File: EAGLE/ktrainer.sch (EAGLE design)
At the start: 21 parts, among them IC1 DS3231/SO

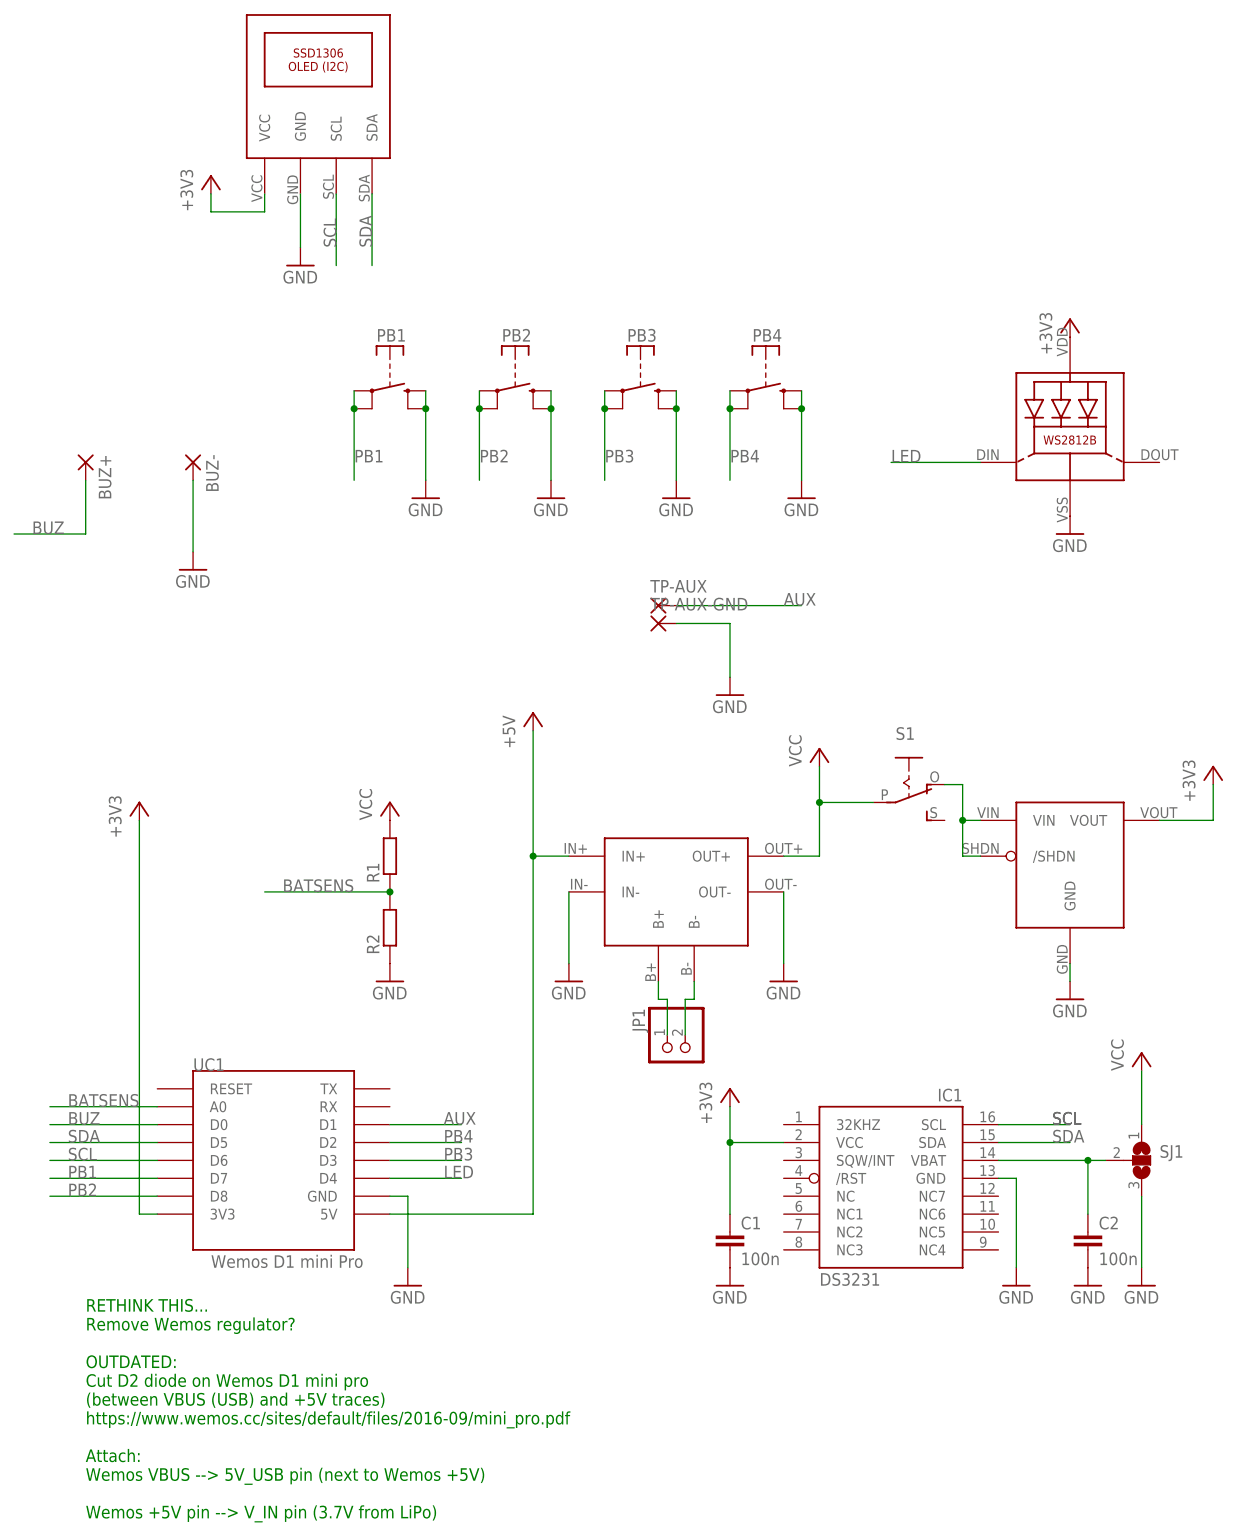
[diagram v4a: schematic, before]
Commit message: Finish work on PCB, create gerber files and order on Seeed Studio
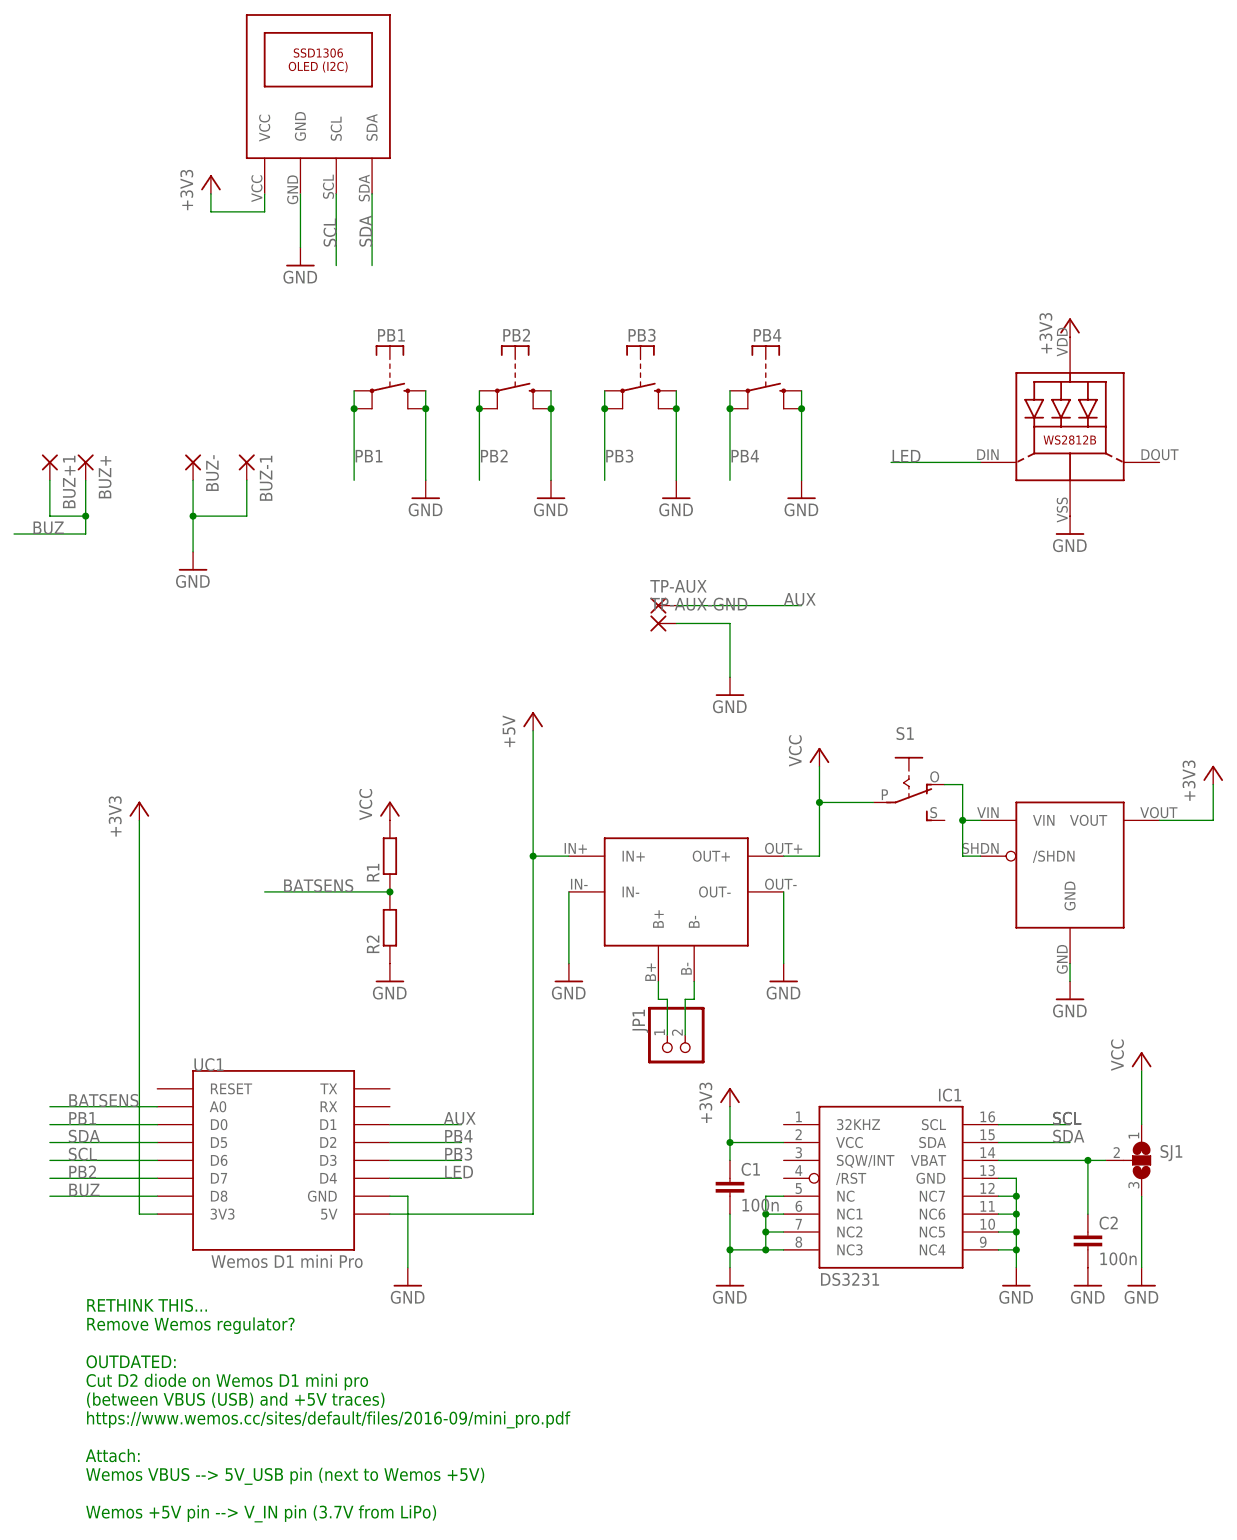
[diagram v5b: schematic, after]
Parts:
- added BUZ+1, BUZ-1: (no value), wirepad:SMD2
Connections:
- net N$6 renamed B-
- net BUZ: now also BUZ+1.P, UC1.D8; no longer UC1.D0
- net GND: now also BUZ-1.P, IC1.NC, IC1.NC1, IC1.NC2, IC1.NC3, IC1.NC4, IC1.NC5, IC1.NC6, IC1.NC7
- net PB1: now also UC1.D0; no longer UC1.D7
- net PB2: now also UC1.D7; no longer UC1.D8
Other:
- moved on the sheet: C1
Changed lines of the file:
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@@
 <part name="TP-AUX" library="wirepad" deviceset="SMD2" device=""/>
 <part name="TP-AUX-GND" library="wirepad" deviceset="SMD2" device=""/>
+<part name="BUZ+1" library="wirepad" deviceset="SMD2" device=""/>
+<part name="BUZ-1" library="wirepad" deviceset="SMD2" device=""/>
 </parts>
 <sheets>
@@
 <instance part="+3V5" gate="G$1" x="175.26" y="129.54"/>
 <instance part="P+2" gate="VCC" x="165.1" y="88.9"/>
-<instance part="C1" gate="G$1" x="106.68" y="63.5"/>
+<instance part="C1" gate="G$1" x="106.68" y="71.12"/>
 <instance part="GND12" gate="1" x="106.68" y="55.88"/>
 <instance part="C2" gate="G$1" x="157.48" y="63.5"/>
@@
 <instance part="TP-AUX" gate="1" x="96.52" y="152.4"/>
 <instance part="TP-AUX-GND" gate="1" x="96.52" y="149.86"/>
+<instance part="BUZ+1" gate="1" x="10.16" y="172.72" rot="R270"/>
+<instance part="BUZ-1" gate="1" x="38.1" y="172.72" rot="R270"/>
 </instances>
 <busses>
@@
 <pinref part="IC1" gate="G$1" pin="GND"/>
 <pinref part="GND8" gate="1" pin="GND"/>
-<wire x1="147.32" y1="58.42" x2="147.32" y2="71.12" width="0.1524" layer="91"/>
+<wire x1="147.32" y1="58.42" x2="147.32" y2="60.96" width="0.1524" layer="91"/>
+<wire x1="147.32" y1="60.96" x2="147.32" y2="63.5" width="0.1524" layer="91"/>
+<wire x1="147.32" y1="63.5" x2="147.32" y2="66.04" width="0.1524" layer="91"/>
+<wire x1="147.32" y1="66.04" x2="147.32" y2="68.58" width="0.1524" layer="91"/>
+<wire x1="147.32" y1="68.58" x2="147.32" y2="71.12" width="0.1524" layer="91"/>
 <wire x1="147.32" y1="71.12" x2="144.78" y2="71.12" width="0.1524" layer="91"/>
+<pinref part="IC1" gate="G$1" pin="NC7"/>
+<wire x1="144.78" y1="68.58" x2="147.32" y2="68.58" width="0.1524" layer="91"/>
+<pinref part="IC1" gate="G$1" pin="NC6"/>
+<wire x1="144.78" y1="66.04" x2="147.32" y2="66.04" width="0.1524" layer="91"/>
+<pinref part="IC1" gate="G$1" pin="NC5"/>
+<wire x1="144.78" y1="63.5" x2="147.32" y2="63.5" width="0.1524" layer="91"/>
+<pinref part="IC1" gate="G$1" pin="NC4"/>
+<wire x1="144.78" y1="60.96" x2="147.32" y2="60.96" width="0.1524" layer="91"/>
+<junction x="147.32" y="68.58"/>
+<junction x="147.32" y="66.04"/>
+<junction x="147.32" y="63.5"/>
+<junction x="147.32" y="60.96"/>
 </segment>
 <segment>
@@
 <pinref part="C1" gate="G$1" pin="2"/>
 <pinref part="GND12" gate="1" pin="GND"/>
+<wire x1="106.68" y1="66.04" x2="106.68" y2="60.96" width="0.1524" layer="91"/>
+<pinref part="IC1" gate="G$1" pin="NC"/>
+<wire x1="106.68" y1="60.96" x2="106.68" y2="58.42" width="0.1524" layer="91"/>
+<wire x1="114.3" y1="68.58" x2="111.76" y2="68.58" width="0.1524" layer="91"/>
+<wire x1="111.76" y1="68.58" x2="111.76" y2="66.04" width="0.1524" layer="91"/>
+<pinref part="IC1" gate="G$1" pin="NC3"/>
+<wire x1="111.76" y1="63.5" x2="111.76" y2="60.96" width="0.1524" layer="91"/>
+<wire x1="111.76" y1="60.96" x2="114.3" y2="60.96" width="0.1524" layer="91"/>
+<pinref part="IC1" gate="G$1" pin="NC2"/>
+<wire x1="114.3" y1="63.5" x2="111.76" y2="63.5" width="0.1524" layer="91"/>
+<pinref part="IC1" gate="G$1" pin="NC1"/>
+<wire x1="114.3" y1="66.04" x2="111.76" y2="66.04" width="0.1524" layer="91"/>
+<wire x1="111.76" y1="66.04" x2="111.76" y2="63.5" width="0.1524" layer="91"/>
+<wire x1="111.76" y1="60.96" x2="106.68" y2="60.96" width="0.1524" layer="91"/>
+<junction x="106.68" y="60.96"/>
+<junction x="111.76" y="60.96"/>
+<junction x="111.76" y="63.5"/>
+<junction x="111.76" y="66.04"/>
 </segment>
 <segment>
@@
 <pinref part="GND15" gate="1" pin="GND"/>
 <pinref part="BUZ-" gate="1" pin="P"/>
-<wire x1="30.48" y1="170.18" x2="30.48" y2="160.02" width="0.1524" layer="91"/>
+<wire x1="30.48" y1="170.18" x2="30.48" y2="165.1" width="0.1524" layer="91"/>
+<pinref part="BUZ-1" gate="1" pin="P"/>
+<wire x1="30.48" y1="165.1" x2="30.48" y2="160.02" width="0.1524" layer="91"/>
+<wire x1="38.1" y1="170.18" x2="38.1" y2="165.1" width="0.1524" layer="91"/>
+<wire x1="38.1" y1="165.1" x2="30.48" y2="165.1" width="0.1524" layer="91"/>
+<junction x="30.48" y="165.1"/>
 </segment>
 <segment>
@@
 </segment>
 <segment>
-<pinref part="UC1" gate="D1" pin="D7"/>
-<wire x1="25.4" y1="71.12" x2="10.16" y2="71.12" width="0.1524" layer="91"/>
-<label x="12.7" y="71.12" size="1.778" layer="95"/>
+<pinref part="UC1" gate="D1" pin="D0"/>
+<wire x1="25.4" y1="78.74" x2="10.16" y2="78.74" width="0.1524" layer="91"/>
+<label x="12.7" y="78.74" size="1.778" layer="95"/>
 </segment>
 </net>
@@
 </segment>
 <segment>
-<pinref part="UC1" gate="D1" pin="D8"/>
-<wire x1="25.4" y1="68.58" x2="10.16" y2="68.58" width="0.1524" layer="91"/>
-<label x="12.7" y="68.58" size="1.778" layer="95"/>
+<pinref part="UC1" gate="D1" pin="D7"/>
+<wire x1="25.4" y1="71.12" x2="10.16" y2="71.12" width="0.1524" layer="91"/>
+<label x="12.7" y="71.12" size="1.778" layer="95"/>
 </segment>
 </net>
@@
 <wire x1="106.68" y1="76.2" x2="114.3" y2="76.2" width="0.1524" layer="91"/>
 <pinref part="C1" gate="G$1" pin="1"/>
-<wire x1="106.68" y1="76.2" x2="106.68" y2="66.04" width="0.1524" layer="91"/>
+<wire x1="106.68" y1="76.2" x2="106.68" y2="73.66" width="0.1524" layer="91"/>
 <junction x="106.68" y="76.2"/>
 </segment>
@@
 </segment>
 </net>
-<net name="N$6" class="0">
+<net name="B-" class="0">
 <segment>
 <pinref part="JP1" gate="G$1" pin="2"/>
@@
 <pinref part="BUZ+" gate="1" pin="P"/>
 <wire x1="15.24" y1="162.56" x2="5.08" y2="162.56" width="0.1524" layer="91"/>
-<wire x1="15.24" y1="170.18" x2="15.24" y2="162.56" width="0.1524" layer="91"/>
-</segment>
-<segment>
-<pinref part="UC1" gate="D1" pin="D0"/>
-<wire x1="25.4" y1="78.74" x2="10.16" y2="78.74" width="0.1524" layer="91"/>
-<label x="12.7" y="78.74" size="1.778" layer="95"/>
-</segment>
-</net>
+<wire x1="15.24" y1="170.18" x2="15.24" y2="165.1" width="0.1524" layer="91"/>
+<pinref part="BUZ+1" gate="1" pin="P"/>
+<wire x1="15.24" y1="165.1" x2="15.24" y2="162.56" width="0.1524" layer="91"/>
+<wire x1="10.16" y1="170.18" x2="10.16" y2="165.1" width="0.1524" layer="91"/>
+<wire x1="10.16" y1="165.1" x2="15.24" y2="165.1" width="0.1524" layer="91"/>
+<junction x="15.24" y="165.1"/>
+</segment>
+<segment>
+<pinref part="UC1" gate="D1" pin="D8"/>
+<wire x1="25.4" y1="68.58" x2="10.16" y2="68.58" width="0.1524" layer="91"/>
+<label x="12.7" y="68.58" size="1.778" layer="95"/>
+</segment>
+</net>

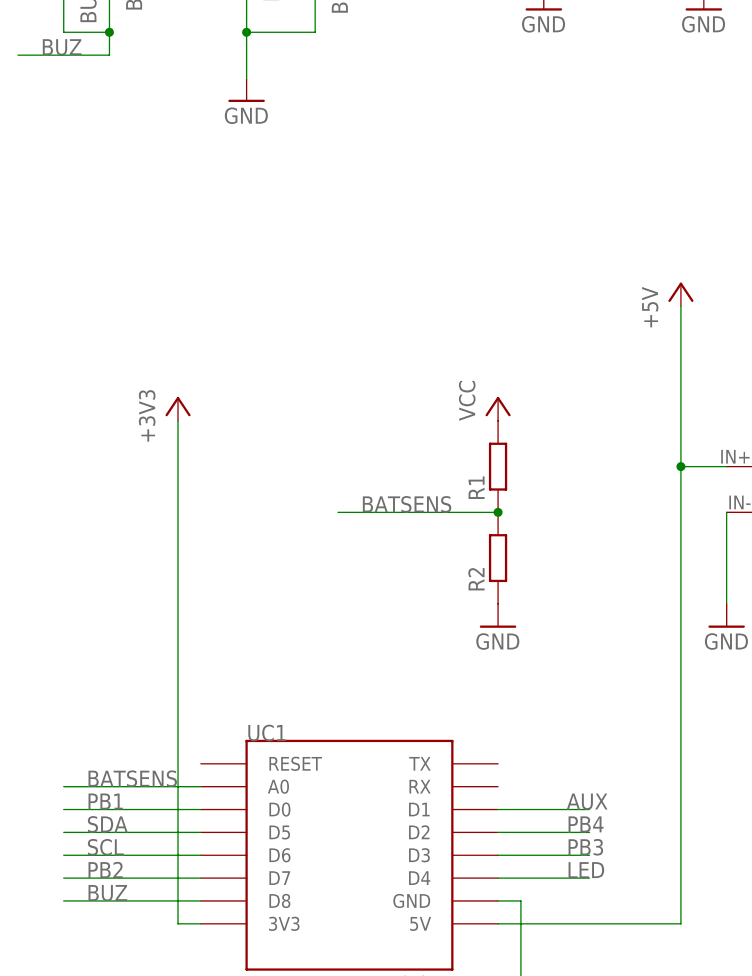
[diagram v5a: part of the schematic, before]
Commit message: Annotate schematic: jumper wire from D1 to D0
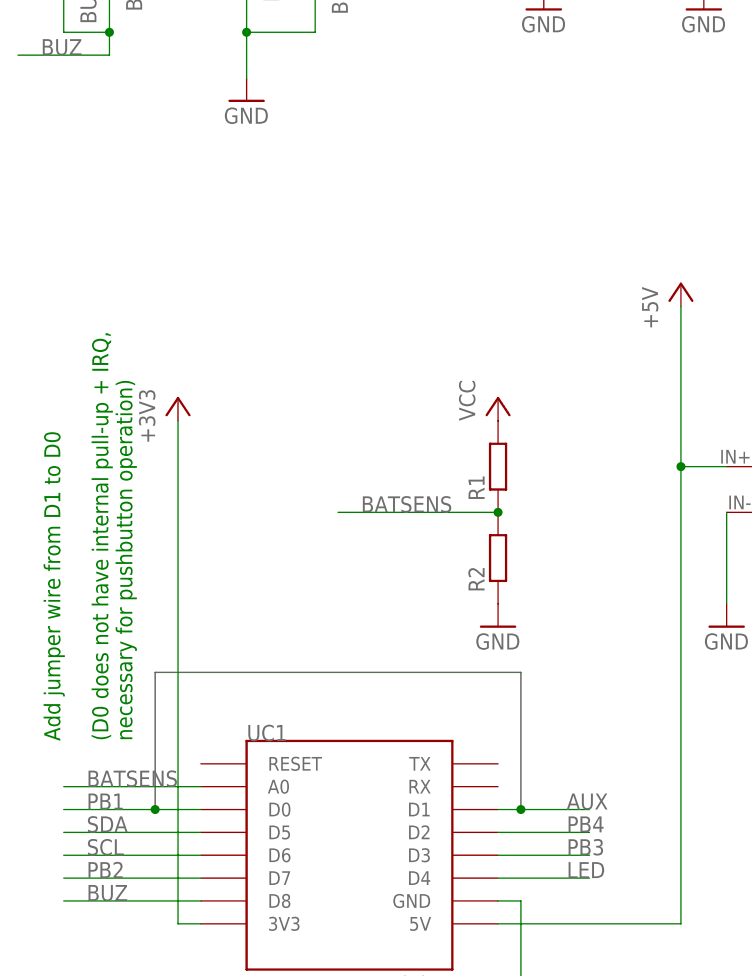
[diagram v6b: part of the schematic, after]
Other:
- note added: "Add jumper wire from D1 to D0 (D0 does not have internal pull-up + IRQ, necessary for pushbutton operation)"
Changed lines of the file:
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@@
 Wemos VBUS --&gt; 5V_USB pin (next to Wemos +5V)
 Wemos +5V pin --&gt; V_IN pin (3.7V from LiPo)</text>
+<wire x1="20.32" y1="78.74" x2="20.32" y2="93.98" width="0.1524" layer="97"/>
+<wire x1="20.32" y1="93.98" x2="60.96" y2="93.98" width="0.1524" layer="97"/>
+<wire x1="60.96" y1="93.98" x2="60.96" y2="78.74" width="0.1524" layer="97"/>
+<text x="17.78" y="86.36" size="1.778" layer="91" rot="R90">Add jumper wire from D1 to D0
+(D0 does not have internal pull-up + IRQ,
+necessary for pushbutton operation)</text>
 </plain>
 <instances>
@@
 <segment>
 <pinref part="UC1" gate="D1" pin="D0"/>
-<wire x1="25.4" y1="78.74" x2="10.16" y2="78.74" width="0.1524" layer="91"/>
+<wire x1="25.4" y1="78.74" x2="20.32" y2="78.74" width="0.1524" layer="91"/>
 <label x="12.7" y="78.74" size="1.778" layer="95"/>
+<junction x="20.32" y="78.74"/>
+<wire x1="20.32" y1="78.74" x2="10.16" y2="78.74" width="0.1524" layer="91"/>
 </segment>
 </net>
@@
 <segment>
 <pinref part="UC1" gate="D1" pin="D1"/>
-<wire x1="58.42" y1="78.74" x2="68.58" y2="78.74" width="0.1524" layer="91"/>
+<wire x1="58.42" y1="78.74" x2="60.96" y2="78.74" width="0.1524" layer="91"/>
 <label x="66.04" y="78.74" size="1.778" layer="95"/>
-</segment>
-</net>
+<junction x="60.96" y="78.74"/>
+<wire x1="60.96" y1="78.74" x2="68.58" y2="78.74" width="0.1524" layer="91"/>
+</segment>
+</net>

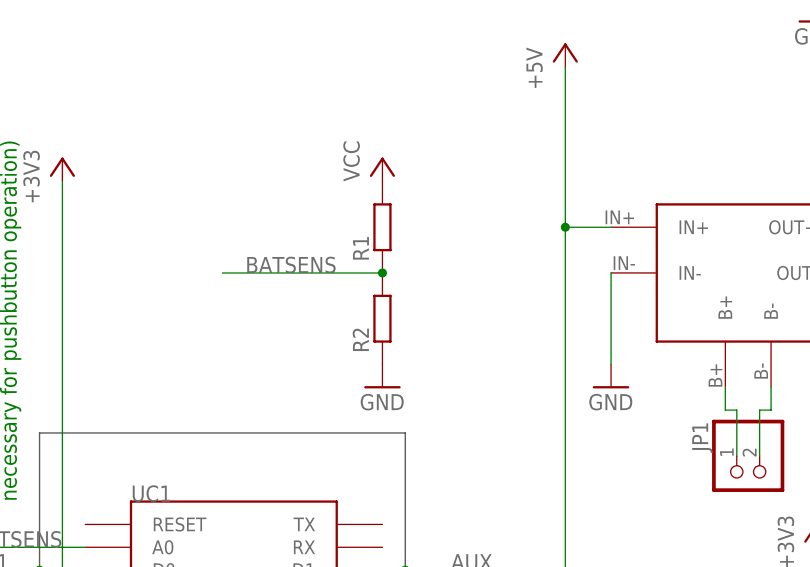
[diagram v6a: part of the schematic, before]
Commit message: Set resistor values for ADC voltage divider
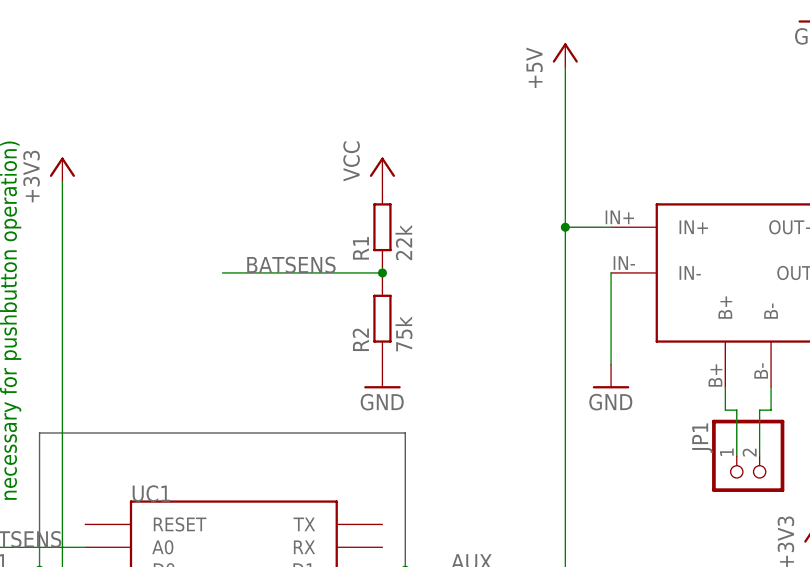
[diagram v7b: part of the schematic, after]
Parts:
- R1: value (none) -> 22k
- R2: value (none) -> 75k
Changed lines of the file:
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@@
 <?xml version="1.0" encoding="utf-8"?>
 <!DOCTYPE eagle SYSTEM "eagle.dtd">
-<eagle version="6.5.0">
+<eagle version="8.3.1">
 <drawing>
 <settings>
 <setting alwaysvectorfont="no"/>
+<setting keepoldvectorfont="yes"/>
 <setting verticaltext="up"/>
 </settings>
@@
 <part name="GND14" library="supply1" deviceset="GND" device=""/>
 <part name="GND15" library="supply1" deviceset="GND" device=""/>
-<part name="R1" library="rcl" deviceset="R-EU_" device="R0805"/>
-<part name="R2" library="rcl" deviceset="R-EU_" device="R0805"/>
+<part name="R1" library="rcl" deviceset="R-EU_" device="R0805" value="22k"/>
+<part name="R2" library="rcl" deviceset="R-EU_" device="R0805" value="75k"/>
 <part name="GND16" library="supply1" deviceset="GND" device=""/>
 <part name="P+3" library="supply1" deviceset="VCC" device=""/>
